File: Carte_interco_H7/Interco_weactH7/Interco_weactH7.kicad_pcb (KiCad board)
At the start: 4 copper layers, 98.4 x 95.3 mm, 112 parts, among them J101 servo orientation, J102 servo bras, J103 servo dicristaline, J104 servo dicristaline, J105 POW_access, J106 KK-254_AE-6410-07A, J107 LIDAR, J108 LIDAR, J109 SNDBOARD, J110 electroaimant, J111 SWrobot, J112 Tirette, J113 pompe, J114 SWcote, J115 reset, J116 vanne, J117 Conn_02x07_Odd_Even, J118 servo orientation, J119 servo bras, J301 629105150521, J302 Conn_01x06_Pin, J401 KK-254_AE-6410-04A, J402 KK-254_AE-6410-04A, Q101 SW_pompe, Q102 SW_pompe, Q103 SW_vanne, Q301 MMBTA44, U101 LD1117S33TR_SOT223, U301 ECMF02-2AMX6, U302 LD1117S33TR_SOT223, U303 STM32F103CBT6, U401 TMC2209, U402 TMC2209, Y301 8MHz

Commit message: WIP. layout ok
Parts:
- removed D101, D102, D103: 1N4007, Diode_THT:D_DO-41_SOD81_P10.16mm_Horizontal
- removed J113: pompe, Connector_Molex:Molex_KK-254_AE-6410-02A_1x02_P2.54mm_Vertical
- removed Q101, Q102: SW_pompe, Package_TO_SOT_THT:TO-220-3_Vertical
- removed Q103: SW_vanne, Package_TO_SOT_THT:TO-220-3_Vertical
- removed R101, R102, R105, R106: 330, Capacitor_SMD:C_0805_2012Metric_Pad1.18x1.45mm_HandSolder
- removed R103, R104, R107, R108: 1k, Capacitor_SMD:C_0805_2012Metric_Pad1.18x1.45mm_HandSolder
- added J120: SWrobot, Connector_Molex:Molex_KK-254_AE-6410-02A_1x02_P2.54mm_Vertical, F.Cu at (87.4, 43.9)
- added J121: reset, Connector_Molex:Molex_KK-254_AE-6410-02A_1x02_P2.54mm_Vertical, F.Cu at (101.1, 43.9)
- J110: value electroaimant -> servo orientation; footprint Connector_Molex:Molex_KK-254_AE-6410-02A_1x02_P2.54mm_Vertical -> Connector_Molex:Molex_KK-254_AE-6410-03A_1x03_P2.54mm_Vertical
- J111: value SWrobot -> servo bras; footprint Connector_Molex:Molex_KK-254_AE-6410-02A_1x02_P2.54mm_Vertical -> Connector_Molex:Molex_KK-254_AE-6410-03A_1x03_P2.54mm_Vertical
- J116: value vanne -> SWcote
- moved J115 104.0 mm to (94.3, 43.9)
- moved J116 96.9 mm to (121.6, 43.9), turned to 90 degrees
- moved J114 89.5 mm to (114.8, 43.9), turned to 90 degrees
- moved J112 87.8 mm to (108.0, 43.9)
- moved J110 80.4 mm to (127.0, 64.5), turned to -90 degrees
- moved J111 59.4 mm to (119.1, 64.5), turned to -90 degrees
- moved C110 16.5 mm to (124.7, 53.4), turned to 90 degrees
- moved J119 14.0 mm to (127.5, 52.4), turned to -90 degrees
- moved J109 9.53 mm to (115.8, 114.6), turned to 0 degrees
- moved C109 7.25 mm to (121.9, 53.4), turned to 90 degrees
- moved J118 7.23 mm to (118.8, 52.4), turned to -90 degrees
- moved R207 7.16 mm to (82.7, 44.6)
- moved D203 7.06 mm to (82.7, 41.0)
- moved R208 6.05 mm to (80.8, 44.6)
- moved D204 5.93 mm to (80.8, 41.0)
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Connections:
- J110 pad 1: Net-(D101-A) -> GND
- J110 pad 2: Net-(D101-K) -> +5V_PWR
- J111 pad 1: /SW_3V3 -> GND
- J111 pad 2: Net-(J111-Pin_2) -> +5V_PWR
- J112 pad 1: /SW_3V3 -> /WEACT/PE0
- J112 pad 2: Net-(J112-Pin_2) -> GND
- J114 pad 1: /SW_3V3 -> /WEACT/PB8
- J114 pad 2: Net-(J114-Pin_2) -> GND
- J115 pad 1: /SW_3V3 -> /WEACT/PB9
- J115 pad 2: Net-(J115-Pin_2) -> GND
- J116 pad 1: Net-(D103-A) -> /WEACT/PB6
- J116 pad 2: Net-(D103-K) -> GND
- U201 pad P1_3: unconnected-(U201A-PE1-PadP1_3) -> /WEACT/PE1
- U201 pad P1_4: unconnected-(U201A-PE0-PadP1_4) -> /WEACT/PE0
- U201 pad P1_5: unconnected-(U201A-PB9-PadP1_5) -> /WEACT/PB9
- U201 pad P1_6: unconnected-(U201A-PB8-PadP1_6) -> /WEACT/PB8
- U201 pad P1_7: unconnected-(U201A-PB7-PadP1_7) -> /WEACT/PB7
- U201 pad P1_8: unconnected-(U201A-PB6-PadP1_8) -> /WEACT/PB6
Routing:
- net +5V_LOGIC: track 190.8 -> 142.1 mm
- net /WEACT/PB7: track 0.00 -> 31.4 mm
- net /WEACT/PB9: track 0.00 -> 27.0 mm
- net /WEACT/PB6: track 0.00 -> 23.9 mm
- net /WEACT/PE0: track 0.00 -> 17.2 mm
- net /WEACT/PB8: track 0.00 -> 16.6 mm
- net /WEACT/PE1: track 0.00 -> 15.5 mm
- net +5V_PWR: track 134.2 -> 148.8 mm
- net /PWM_SERVO6: track 9.22 -> 19.2 mm
- net GND: track 244.1 -> 238.4 mm
- net /SB_RX: track 14.5 -> 19.1 mm
- net /SB_RST: track 15.5 -> 13.0 mm
- net +BATT: track 103.0 -> 101.8 mm
- net /PWM_SERVO5: track 14.3 -> 13.2 mm
- net /SB_TX: track 18.1 -> 19.1 mm
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
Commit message: ready for check
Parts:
- removed D303: PMEG40T10ER, Diode_SMD:Nexperia_CFP3_SOD-123W
- moved R305 5.59 mm to (52.1, 48.0)
- moved R204 3.88 mm to (66.3, 112.3), turned to 180 degrees
- moved D304 1.07 mm to (63.5, 51.3)
- moved R203 1.05 mm to (66.3, 114.6), turned to 180 degrees
- moved R301 1.02 mm to (47.2, 48.1)
- moved R302 1.02 mm to (48.8, 48.1)
- moved R303 1.02 mm to (50.3, 48.1)
- moved R312 0.91 mm to (54.4, 54.9)
- moved D302 0.66 mm to (55.9, 49.5)
- moved D202 0.27 mm to (76.7, 41.0)
- moved R206 0.27 mm to (76.7, 44.6)
- moved J302 0.25 mm to (44.2, 68.4)
- moved C104 0.25 mm to (109.7, 128.8)
- moved D201 0.18 mm to (78.7, 41.0)
- moved R205 0.18 mm to (78.7, 44.6)
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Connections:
- J110 pad 3: unconnected-(J110-Pin_3-Pad3) -> /WEACT/PD3
- J111 pad 3: unconnected-(J111-Pin_3-Pad3) -> /WEACT/PD5
- U201 pad P1_1: unconnected-(U201A-GND-PadP1_1) -> GND
- U201 pad P1_14: unconnected-(U201A-PD5-PadP1_14) -> /WEACT/PD5
- U201 pad P1_16: unconnected-(U201A-PD3-PadP1_16) -> /WEACT/PD3
- U201 pad P2_1: unconnected-(U201B-GND-PadP2_1) -> GND
- U201 pad P2_15: unconnected-(U201B-GND-PadP2_15) -> GND
- U201 pad P2_32: /WEACT/TIM1_CH1 -> unconnected-(U201B-PE9-PadP2_32)
- U201 pad P2_34: /WEACT/TIM1_CH2 -> unconnected-(U201B-PE11-PadP2_34)
- U201 pad P2_36: /WEACT/TIM1_CH3 -> unconnected-(U201B-PE13-PadP2_36)
- U201 pad P2_37: /WEACT/TIM1_CH4 -> unconnected-(U201B-PE14-PadP2_37)
- U201 pad P2_38: /WEACT/PE15 -> unconnected-(U201B-PE15-PadP2_38)
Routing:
- net +5V_LOGIC: track 142.1 -> 250.0 mm
- net GND: track 238.4 -> 315.1 mm, vias 39 -> 89
- net +3V3: track 84.6 -> 109.6 mm, vias 2 -> 0
- net /WEACT/PD3: track 0.00 -> 16.8 mm
- net +5V_PWR: track 148.8 -> 158.3 mm
- net /WEACT/PD5: track 0.00 -> 8.34 mm
- net /PWM_SERVO4: track 38.7 -> 45.0 mm
- net Net-(D302-A): track 13.4 -> 7.18 mm
- net /WEACT/TIM5_CH1: track 49.4 -> 55.2 mm
- net /WEACT/UART7_TX: track 7.39 -> 12.3 mm
- net /PWM_SERVO2: track 34.6 -> 30.1 mm
- net Net-(Q301-B): track 12.5 -> 16.9 mm
- net /PWM_SERVO3: track 42.0 -> 38.6 mm
- net /WEACT/TIM2_CH1: track 21.1 -> 17.7 mm
- net +BATT: track 101.8 -> 105.0 mm
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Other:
- board text removed: "Pokibot Carte interco V1.0 - 04/2022"

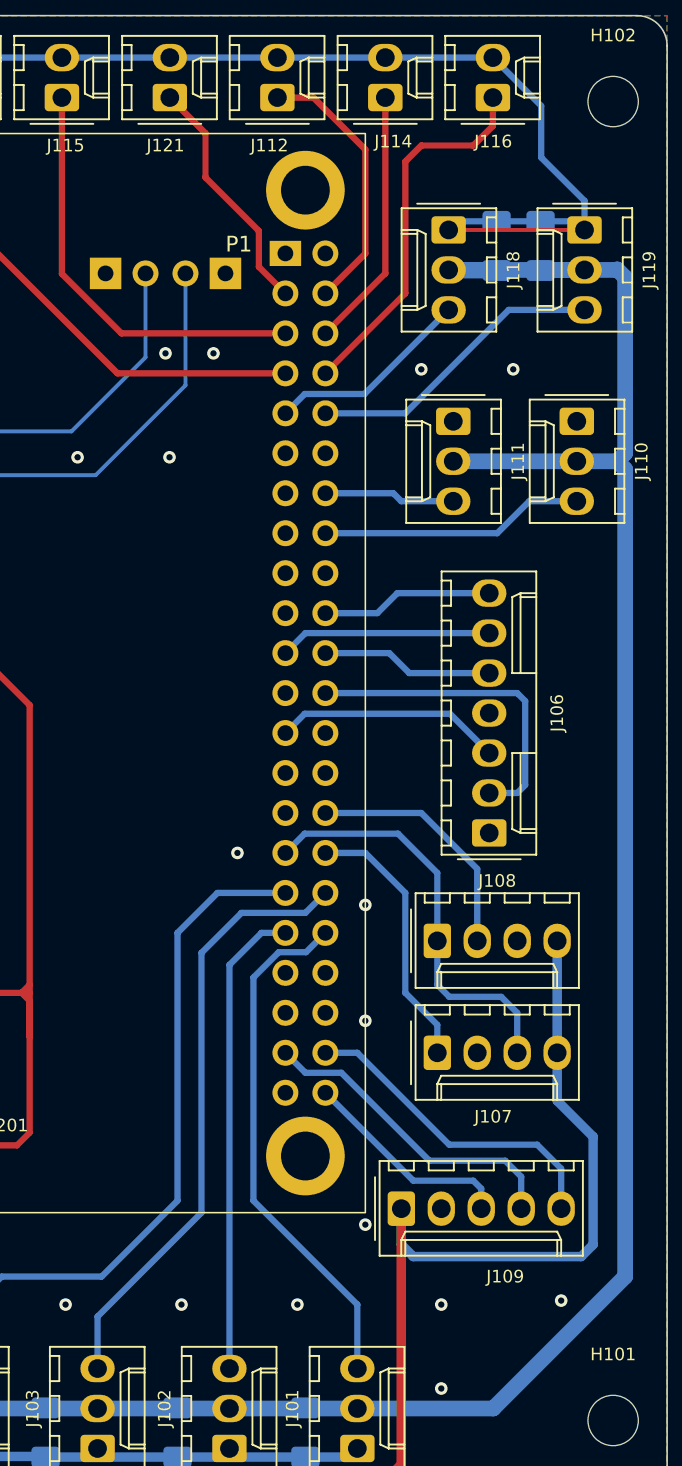
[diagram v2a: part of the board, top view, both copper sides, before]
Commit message: pins in conflict rerouted
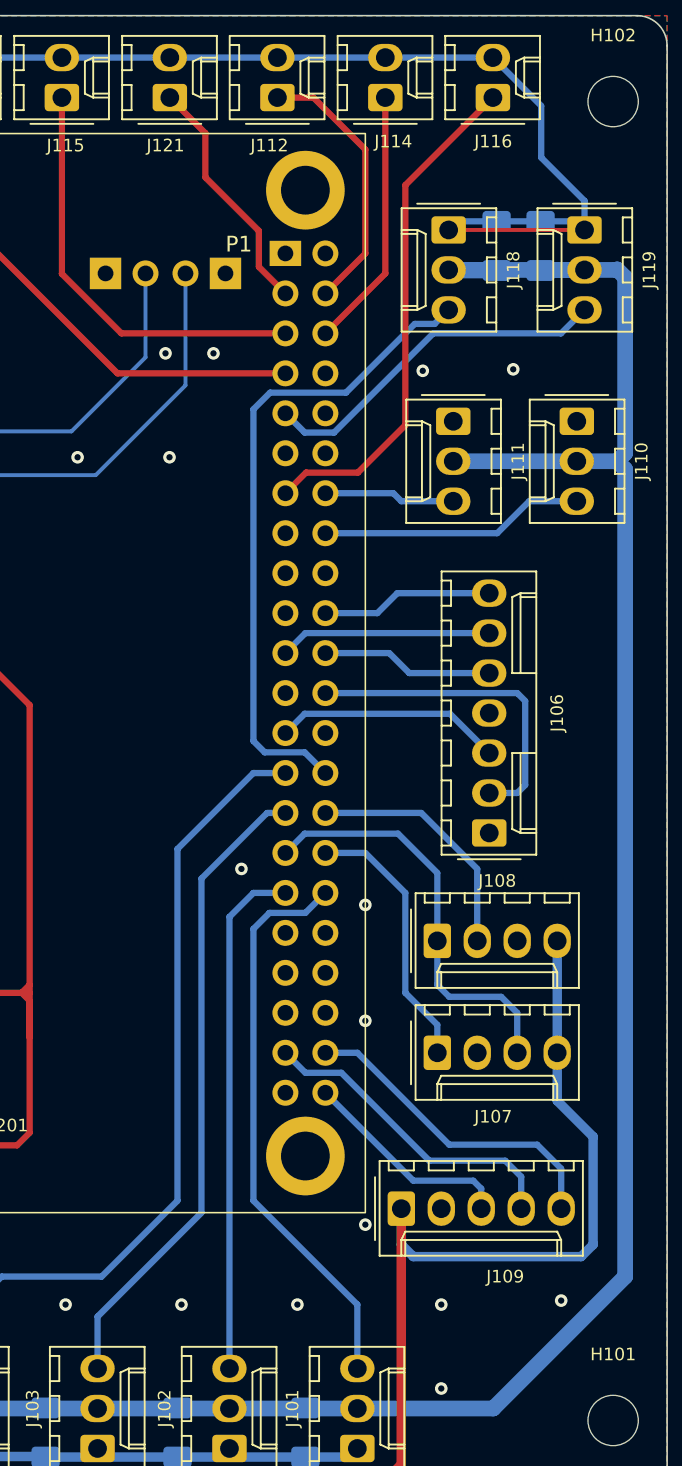
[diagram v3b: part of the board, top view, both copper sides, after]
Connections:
- J116 pad 1: /WEACT/PB6 -> /WEACT/PD6
- U201 pad P1_10: /PWM_SERVO6 -> unconnected-(U201A-PB4-PadP1_10)
- U201 pad P1_13: unconnected-(U201A-PD6-PadP1_13) -> /WEACT/PD6
- U201 pad P1_27: unconnected-(U201A-PA9-PadP1_27) -> /PWM_SERVO4
- U201 pad P1_28: unconnected-(U201A-PA8-PadP1_28) -> /PWM_SERVO5
- U201 pad P1_29: unconnected-(U201A-PC9-PadP1_29) -> /PWM_SERVO3
- U201 pad P1_33: /PWM_SERVO4 -> /PWM_SERVO2
- U201 pad P1_34: /PWM_SERVO3 -> /PWM_SERVO1
- U201 pad P1_35: /PWM_SERVO2 -> unconnected-(U201A-PD13-PadP1_35)
- U201 pad P1_36: /PWM_SERVO1 -> unconnected-(U201A-PD12-PadP1_36)
- U201 pad P1_8: /WEACT/PB6 -> unconnected-(U201A-PB6-PadP1_8)
- U201 pad P1_9: /PWM_SERVO5 -> /PWM_SERVO6
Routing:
- net /WEACT/PD6: track 0.00 -> 32.5 mm
- net /PWM_SERVO5: track 13.1 -> 41.5 mm
- net /WEACT/PB6: track 23.9 -> 0.00 mm
- net /PWM_SERVO4: track 45.0 -> 51.3 mm
- net /PWM_SERVO6: track 19.2 -> 22.7 mm
- net /PWM_SERVO1: track 33.3 -> 36.2 mm
- net /PWM_SERVO2: track 30.1 -> 32.9 mm
- net /PWM_SERVO3: track 38.6 -> 40.9 mm

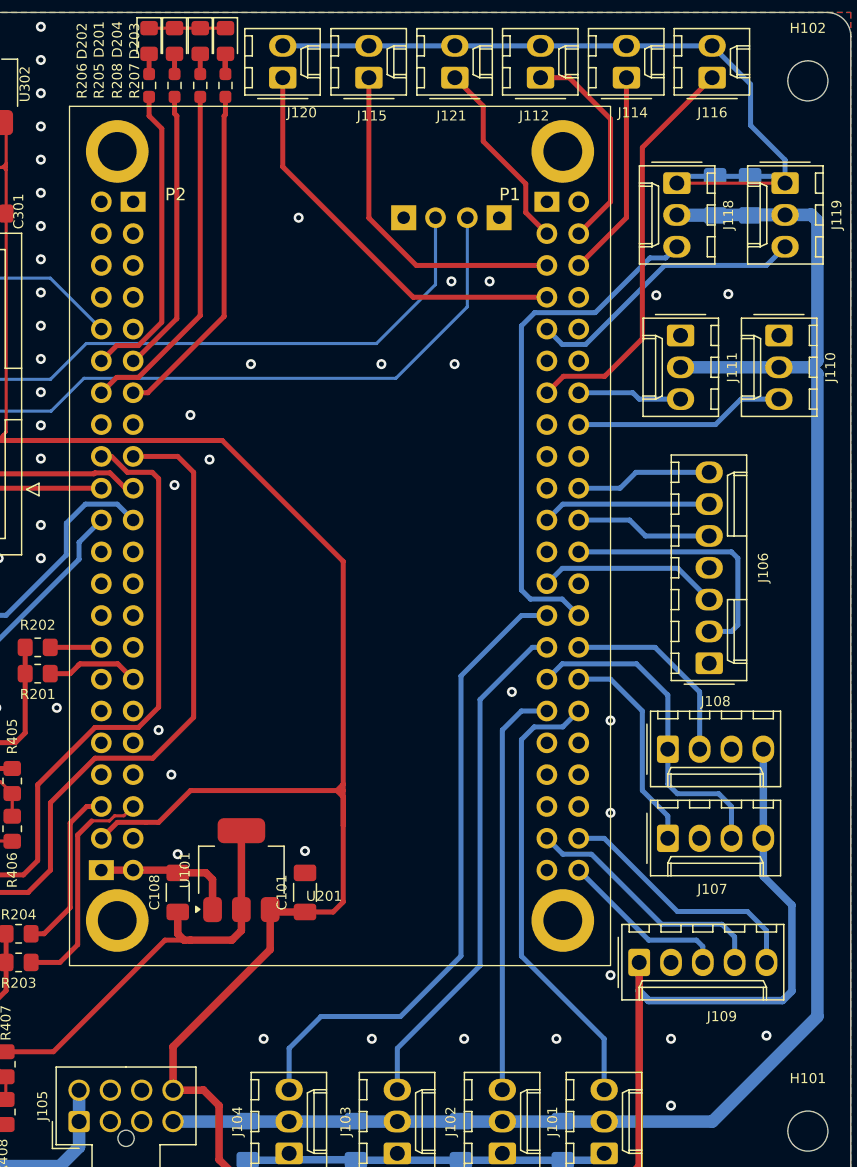
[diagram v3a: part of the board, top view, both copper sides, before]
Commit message: P1 connector was backward
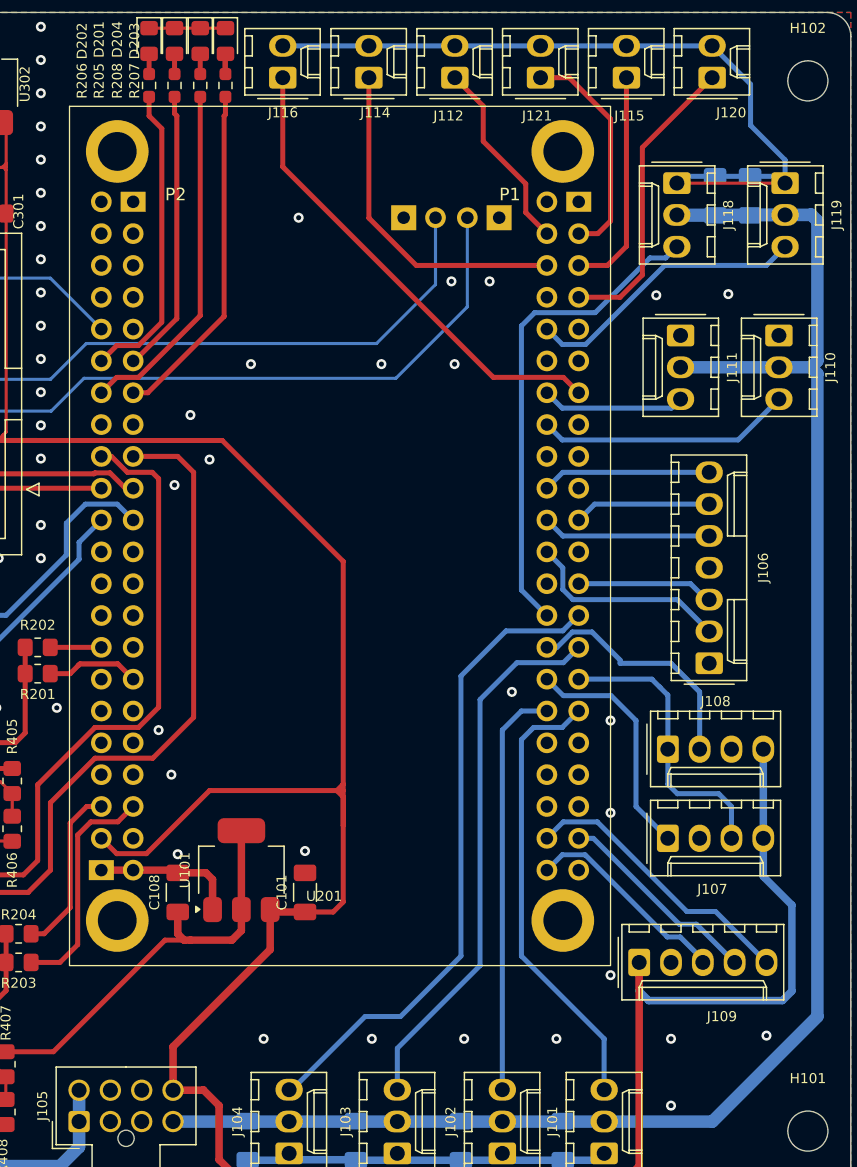
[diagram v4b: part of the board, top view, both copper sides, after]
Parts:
- moved J116 34.3 mm to (87.4, 43.9)
- moved J120 34.3 mm to (121.6, 43.9)
- moved J114 20.6 mm to (94.3, 43.9)
- moved J115 20.6 mm to (114.8, 43.9)
- moved J112 6.84 mm to (101.1, 43.9)
- moved J121 6.84 mm to (108.0, 43.9)
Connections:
- U201 pad P1_33: /PWM_SERVO2 -> /PWM_SERVO1
- U201 pad P1_34: /PWM_SERVO1 -> /PWM_SERVO2
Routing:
- net /WEACT/PB8: track 16.6 -> 27.0 mm
- net /WEACT/PB9: track 27.0 -> 17.9 mm
- net /WEACT/PB7: track 32.5 -> 23.9 mm
- net /WEACT/PD6: track 32.5 -> 38.2 mm
- net /MOTOR_RX(IN): track 20.7 -> 16.6 mm
- net /SB_TX: track 20.3 -> 16.5 mm
- net /WEACT/TIM3_CH3: track 15.7 -> 19.4 mm
- net /LIDAR_TX: track 26.7 -> 23.1 mm
- net /WEACT/PD3: track 16.8 -> 20.4 mm
- net /MOTOR_TX(OUT): track 14.5 -> 10.9 mm
- net /WEACT/PD5: track 8.34 -> 11.5 mm
- net /SB_RST: track 13.7 -> 16.6 mm
- net /WEACT/PE1: track 15.5 -> 18.0 mm
- net /PWM_SERVO3: track 40.9 -> 43.5 mm
- net /MOTOR_SCK: track 10.9 -> 13.5 mm
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
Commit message: send PCB
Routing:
- net /PWM_SERVO6: track 22.7 -> 19.2 mm
- removed copper zone on In1.Cu, net GND
- removed copper zone on In2.Cu, net GND
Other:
- copper layers 4 -> 2
